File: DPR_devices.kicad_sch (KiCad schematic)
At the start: 0 parts

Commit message: Added all 3 ADC and routed them to RP2040 !
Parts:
- added C37, C40, C41, C42, C45, C46, C47, C50, C51: 1u, symbol Device:C
- added C38, C43, C48: 10u, symbol Device:C
- added C39, C44, C49: 4.7u, symbol Device:C
- added U7, U8, U9: ADS8681IPW, symbol DPR_devices:ADS8681IPW_
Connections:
- new net: C47.1, C48.2, U9.6 (REFCAP)
- new net: C47.2, U9.5 (REFGND)
- new net: C37.1, C38.2, U7.6 (REFCAP)
- new net: C37.2, U7.5 (REFGND)
- new net: C42.2, U8.5 (REFGND)
- new net: C42.1, C43.2, U8.6 (REFCAP)
- new net +3V3: C41.2, C46.2, C51.2, U7.16 (DVDD), U8.16 (DVDD), U9.16 (DVDD)
- new net +5V: C40.1, C45.1, C50.1, U7.2 (AVDD), U8.2 (AVDD), U9.2 (AVDD)
- new net ADC_REF: C39.1, C44.1, C49.1, U7.4 (REFIO), U8.4 (REFIO), U9.4 (REFIO)
- new net ADC_RESET: U7.9 (RST), U8.9 (RST), U9.9 (RST)
- new net CS_ADC1: U7.11 (CONVST/CS)
- new net CS_ADC2: U8.11 (CONVST/CS)
- new net CS_ADC3: U9.11 (CONVST/CS)
- new net GND: C38.1, C39.2, C40.2, C41.1, C43.1, C44.2, C45.2, C46.1, C48.1, C49.2, C50.2, C51.1, U7.1 (DGND), U7.3 (AGND), U7.8 (AIN_GND), U8.1 (DGND), U8.3 (AGND), U8.8 (AIN_GND), U9.1 (DGND), U9.3 (AGND), U9.8 (AIN_GND)
- new net MISO: U7.13 (SDO-0), U8.13 (SDO-0), U9.13 (SDO-0)
- new net MOSI: U7.10 (SDI), U8.10 (SDI), U9.10 (SDI)
- new net PD_OUT: U7.7 (AIN_P), U8.7 (AIN_P), U9.7 (AIN_P)
- new net SCLK: U7.12 (SCLK), U8.12 (SCLK), U9.12 (SCLK)
- no-connect marks 0 -> 6

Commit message: Last CPR_devices changes
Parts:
- added C52, C53, C54: 4.7n, symbol Device:C
- added J10: M12_P2, symbol Connector:Conn_01x04_Socket
- added J11: SMA_P3, symbol Connector:Conn_Coaxial
- added J6: M12_P1, symbol Connector:Conn_01x04_Socket
- added J7: M12_P3, symbol Connector:Conn_01x04_Socket
- added J8: SMA_P1, symbol Connector:Conn_Coaxial
- added J9: SMA_P2, symbol Connector:Conn_Coaxial
- added R10, R11, R12: 100R, symbol DPR_devices:R
- added U10: PCA9548APW, Package_SO:TSSOP-24_4.4x7.8mm_P0.65mm, symbol Interface_Expansion:PCA9548APW
- C37, C40, C41, C42, C45, C46, C47, C50, C51: value 1u -> C; footprint (none) -> Capacitor_SMD:C_0402_1005Metric; symbol Device:C -> DPR_devices:C
- C38, C43, C48: value 10u -> C; footprint (none) -> Capacitor_SMD:C_0603_1608Metric; symbol Device:C -> DPR_devices:C
- C39, C44, C49: value 4.7u -> C; footprint (none) -> Capacitor_SMD:C_0603_1608Metric; symbol Device:C -> DPR_devices:C
- U7, U8, U9: footprint (none) -> Package_SO:TSSOP-16_4.4x5mm_P0.65mm
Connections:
- removed net PD_OUT: U7.7 (AIN_P), U8.7 (AIN_P), U9.7 (AIN_P)
- new net +24V: J10.1 (Pin_1), J6.1 (Pin_1), J7.1 (Pin_1)
- new net AGND: C52.1, C53.1, C54.1, J10.3 (Pin_3), J11.2 (Ext), J6.3 (Pin_3), J7.3 (Pin_3), J8.2 (Ext), J9.2 (Ext)
- new net AIN1_P: C52.2, J8.1 (In), R10.2, U7.7 (AIN_P)
- new net AIN2_P: C53.2, J9.1 (In), R11.2, U8.7 (AIN_P)
- new net AIN3_P: C54.2, J11.1 (In), R12.2, U9.7 (AIN_P)
- new net P1_OUT: J6.4 (Pin_4), R10.1
- new net P2_OUT: J10.4 (Pin_4), R11.1
- new net P3_OUT: J7.4 (Pin_4), R12.1
- no-connect marks 6 -> 9

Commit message: Schematic ok (je crois)
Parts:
- added C55: 100n, symbol Device:C
- added J12: Sens. PTE1, symbol Connector:Conn_01x04_Socket
- added J13: Sens. PTE2, symbol Connector:Conn_01x04_Socket
- added J14: Sens. PTE3, symbol Connector:Conn_01x04_Socket
- added R13, R14: 4.7k, symbol DPR_devices:R
- added R22: 10k, symbol DPR_devices:R
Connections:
- net +3V3: now also U10.24 (VCC), C55.2, J12.1 (Pin_1), J13.1 (Pin_1), J14.1 (Pin_1), R13.1, R14.1, R22.1
- net AGND: no longer J10.3 (Pin_3), J6.3 (Pin_3), J7.3 (Pin_3)
- net GND: now also U10.1 (A0), U10.12 (GND), U10.2 (A1), U10.21 (A2), C55.1, J12.2 (Pin_2), J13.2 (Pin_2), J14.2 (Pin_2)
- net I2C_SCL: now reaches U10.22 (SCL)
- net I2C_SCL: now also R13.2
- net I2C_SDA: now reaches U10.23 (SDA)
- net I2C_SDA: now also R14.2
- net at U10.3 (~{RESET}): now also R22.2
- net PTE1_SDA: now reaches U10.4 (SD0)
- net PTE1_SDA: now also J12.4 (Pin_4)
- net PTE1_SCL: now reaches U10.5 (SC0)
- net PTE1_SCL: now also J12.3 (Pin_3)
- net PTE2_SDA: now reaches U10.6 (SD1)
- net PTE2_SDA: now also J13.4 (Pin_4)
- net PTE2_SCL: now reaches U10.7 (SC1)
- net PTE2_SCL: now also J13.3 (Pin_3)
- net PTE3_SDA: now reaches U10.8 (SD2)
- net PTE3_SDA: now also J14.4 (Pin_4)
- net PTE3_SCL: now reaches U10.9 (SC2)
- net PTE3_SCL: now also J14.3 (Pin_3)
- new net GNDD: J10.3 (Pin_3), J6.3 (Pin_3), J7.3 (Pin_3)
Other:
- note added: "ADC x3"
- note added: "Conn. M12 pour Kistler analogique"
- note added: "Multiplexer + Conn. Sensata en I2C"
- note added: "SMA pour oscillo. p.ex"
- moved on the sheet: C37, C38, C39, C40, C41, C42, C43, C44, C45, C46, C47, C48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

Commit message: Last Push pour que tu check, après je commence le Layout
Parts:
- removed J10: M12_P2, symbol Connector:Conn_01x04_Socket
- removed J12: Sens. PTE1, symbol Connector:Conn_01x04_Socket
- removed J13: Sens. PTE2, symbol Connector:Conn_01x04_Socket
- removed J14: Sens. PTE3, symbol Connector:Conn_01x04_Socket
- removed J6: M12_P1, symbol Connector:Conn_01x04_Socket
- removed J7: M12_P3, symbol Connector:Conn_01x04_Socket
- added J12: Sens. P2, KiNic_footprints:M12B05PFFREE0001, symbol KiNic_symbols:M12B-05PFFR-EE0001
- added J13: Sens. P3, KiNic_footprints:M12B05PFFREE0001, symbol KiNic_symbols:M12B-05PFFR-EE0001
- added J17: Sens. P1, KiNic_footprints:M12B05PFFREE0001, symbol KiNic_symbols:M12B-05PFFR-EE0001
- added J6: M12_P1, DPR_devices:M12_NorComp_4Pin_RA, symbol Connector:Conn_01x05_Socket
- added J7: M12_P2, DPR_devices:M12_NorComp_4Pin_RA, symbol Connector:Conn_01x05_Socket
- added J8: M12_P3, DPR_devices:M12_NorComp_4Pin_RA, symbol Connector:Conn_01x05_Socket
- C37, C40, C41, C42, C45, C46, C47, C50, C51: value C -> 1u
- C38, C43, C48: value C -> 10u
- C39, C44, C49: value C -> 4.7u
- C52, C53, C54, C55: footprint (none) -> Capacitor_SMD:C_0402_1005Metric
- J10: renamed from J9; footprint (none) -> Connector_Coaxial:SMA_Amphenol_901-144_Vertical
- J11: footprint (none) -> Connector_Coaxial:SMA_Amphenol_901-144_Vertical
- J9: renamed from J8; footprint (none) -> Connector_Coaxial:SMA_Amphenol_901-144_Vertical
- R10, R11, R12, R13, R14, R22: footprint (none) -> Resistor_SMD:R_0603_1608Metric
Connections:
- net +24V: now also J6.1 (Pin_1), J7.1 (Pin_1), J8.1 (Pin_1)
- net +5V: now also J12.4, J13.4, J17.4
- net GNDD: now also J12.3, J12.5, J13.3, J13.5, J17.3, J17.5, J6.3 (Pin_3), J6.5 (Pin_5), J7.3 (Pin_3), J7.5 (Pin_5), J8.3 (Pin_3), J8.5 (Pin_5)
- net P1_OUT: now also J6.4 (Pin_4)
- net P2_OUT: now also J7.4 (Pin_4)
- net P3_OUT: now also J8.4 (Pin_4)
- net PTE1_SCL: now also J17.1
- net PTE1_SDA: now also J17.2
- net PTE2_SCL: now also J12.1
- net PTE2_SDA: now also J12.2
- net PTE3_SCL: now also J13.1
- net PTE3_SDA: now also J13.2
- no-connect marks 9 -> 19
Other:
- note added: "SMA (?)"
- note removed: "SMA pour oscillo. p.ex"
- moved on the sheet: C52, C53, C54, J10, J11, J9, R10, R11, R12

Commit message: Finito je te laisse check
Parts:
- removed J6: M12_P1, DPR_devices:M12_NorComp_4Pin_RA, symbol Connector:Conn_01x05_Socket
- removed J7: M12_P2, DPR_devices:M12_NorComp_4Pin_RA, symbol Connector:Conn_01x05_Socket
- removed J8: M12_P3, DPR_devices:M12_NorComp_4Pin_RA, symbol Connector:Conn_01x05_Socket
- added H2, H3, H4: MountingHole, MountingHole:MountingHole_3.2mm_M3, symbol Mechanical:MountingHole
- added J14: Servo1, Connector_PinHeader_2.54mm:PinHeader_1x03_P2.54mm_Vertical, symbol Connector:Conn_01x03_Pin
- added J16: Servo2, Connector_PinHeader_2.54mm:PinHeader_1x03_P2.54mm_Vertical, symbol Connector:Conn_01x03_Pin
- added J20: M12_P2, KiNic_footprints:M12B05PFFREE0001, symbol KiNic_symbols:M12B-05PFFR-EE0001
- added J6: M12_P3, KiNic_footprints:M12B05PFFREE0001, symbol KiNic_symbols:M12B-05PFFR-EE0001
- added J7: M12_P1, KiNic_footprints:M12B05PFFREE0001, symbol KiNic_symbols:M12B-05PFFR-EE0001
- added R23, R24, R25, R26, R27, R28: 4.7k, Resistor_SMD:R_0603_1608Metric, symbol DPR_devices:R
- added R30, R31: 47R, Resistor_SMD:R_0603_1608Metric, symbol DPR_devices:R
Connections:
- net +24V: now also J20.4, J6.4, J7.4
- net +3V3: now also J12.1, J12.2, J13.1, J13.2, J17.1, J17.2, R23.2, R24.2, R25.2, R26.2, R27.2, R28.2
- net GNDD: now also J20.3, J20.5, J6.3, J6.5, J7.3, J7.5
- net P1_OUT: now also J7.1
- net P2_OUT: now also J20.1
- net P3_OUT: now also J6.1
- net PTE1_SCL: now also R27.1; no longer J17.1
- net PTE1_SDA: now also R28.1; no longer J17.2
- net PTE2_SCL: now also R23.1; no longer J12.1
- net PTE2_SDA: now also R24.1; no longer J12.2
- net PTE3_SCL: now also R25.1; no longer J13.1
- net PTE3_SDA: now also R26.1; no longer J13.2
- net RESET: now reaches R22.2, U10.3 (~{RESET})
- new net: J14.3 (Pin_3), R30.1
- new net: J16.3 (Pin_3), R31.1
- new net +8V4_SERVO: J14.2 (Pin_2), J16.2 (Pin_2)
- new net GND_SERVO: J14.1 (Pin_1), J16.1 (Pin_1)
- new net PWM_SERVO1: R30.2
- new net PWM_SERVO2: R31.2
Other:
- note added: "M3"
- note added: "SMA"
- note removed: "SMA (?)"
- moved on the sheet: C55, J12, J13, J17, R13, R14, R22, U10

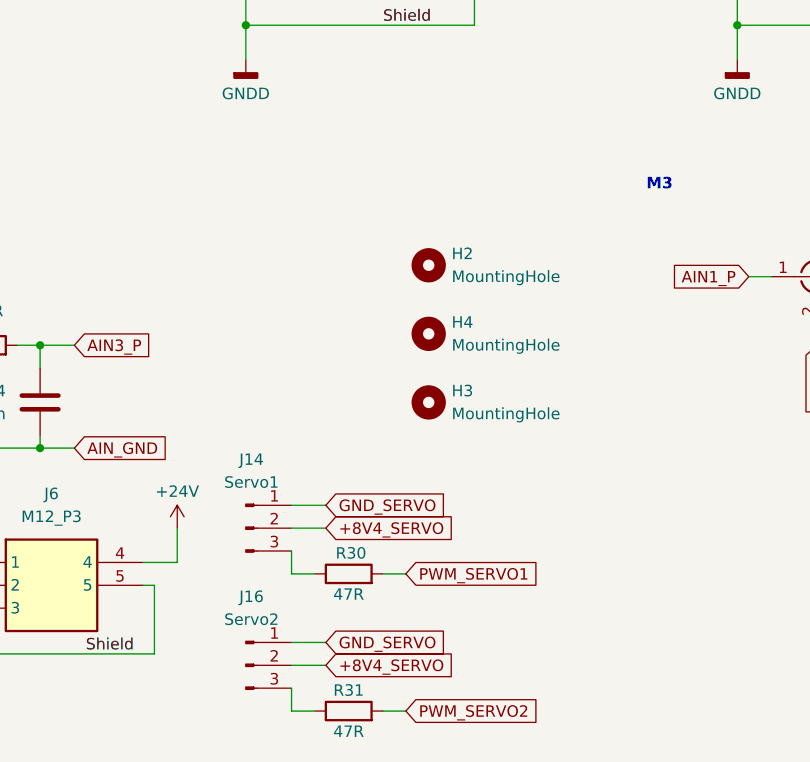
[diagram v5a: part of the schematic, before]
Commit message: added reset and bootsel buttons
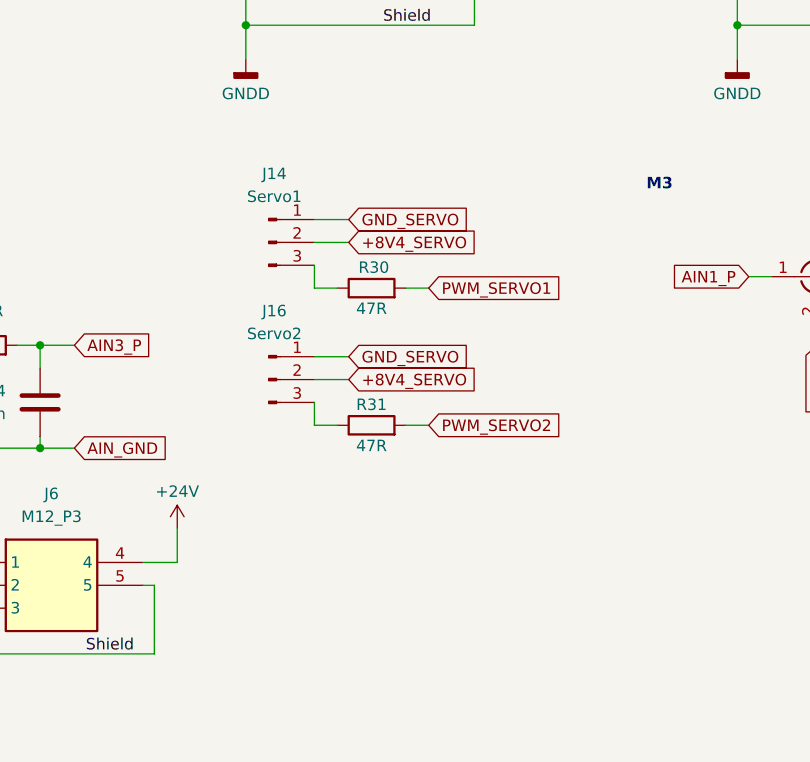
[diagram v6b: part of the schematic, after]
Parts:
- removed H2, H3, H4: MountingHole, MountingHole:MountingHole_3.2mm_M3, symbol Mechanical:MountingHole
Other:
- moved on the sheet: J14, J16, R30, R31

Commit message: last modifications
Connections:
- net AGND is gone; now on net GND: C52.1, C53.1, C54.1, J10.2 (Ext), J11.2 (Ext), J9.2 (Ext)

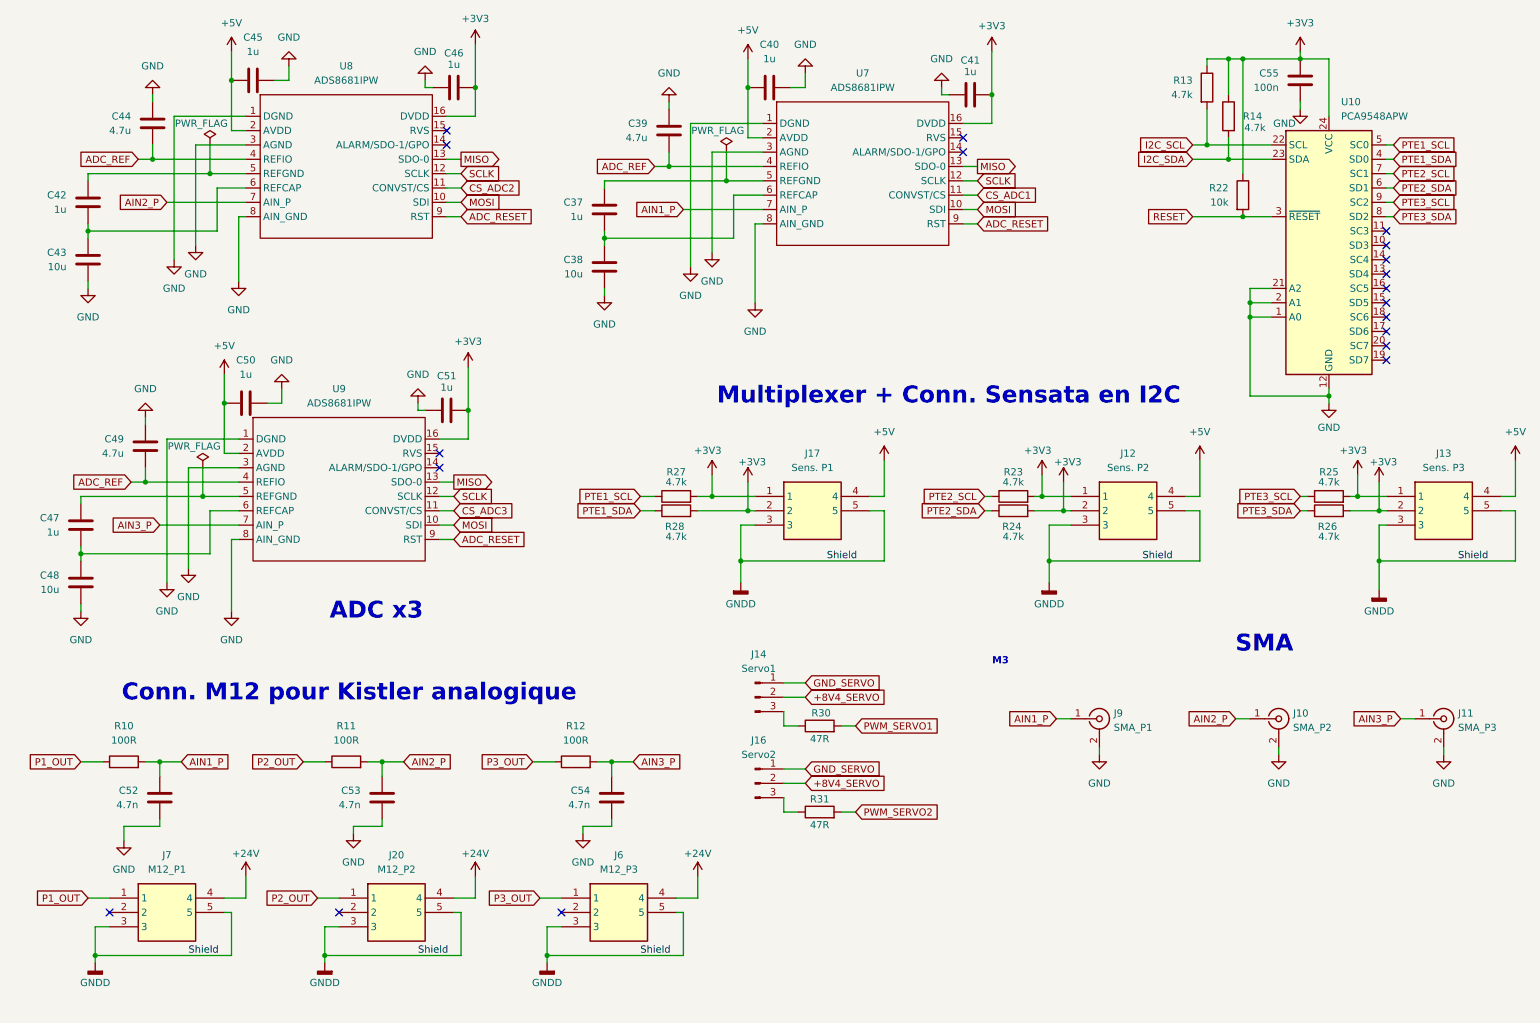
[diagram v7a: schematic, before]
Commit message: Changed M12 for SMA + 2 pins alim. --> we will have to split the cable from Kistlers
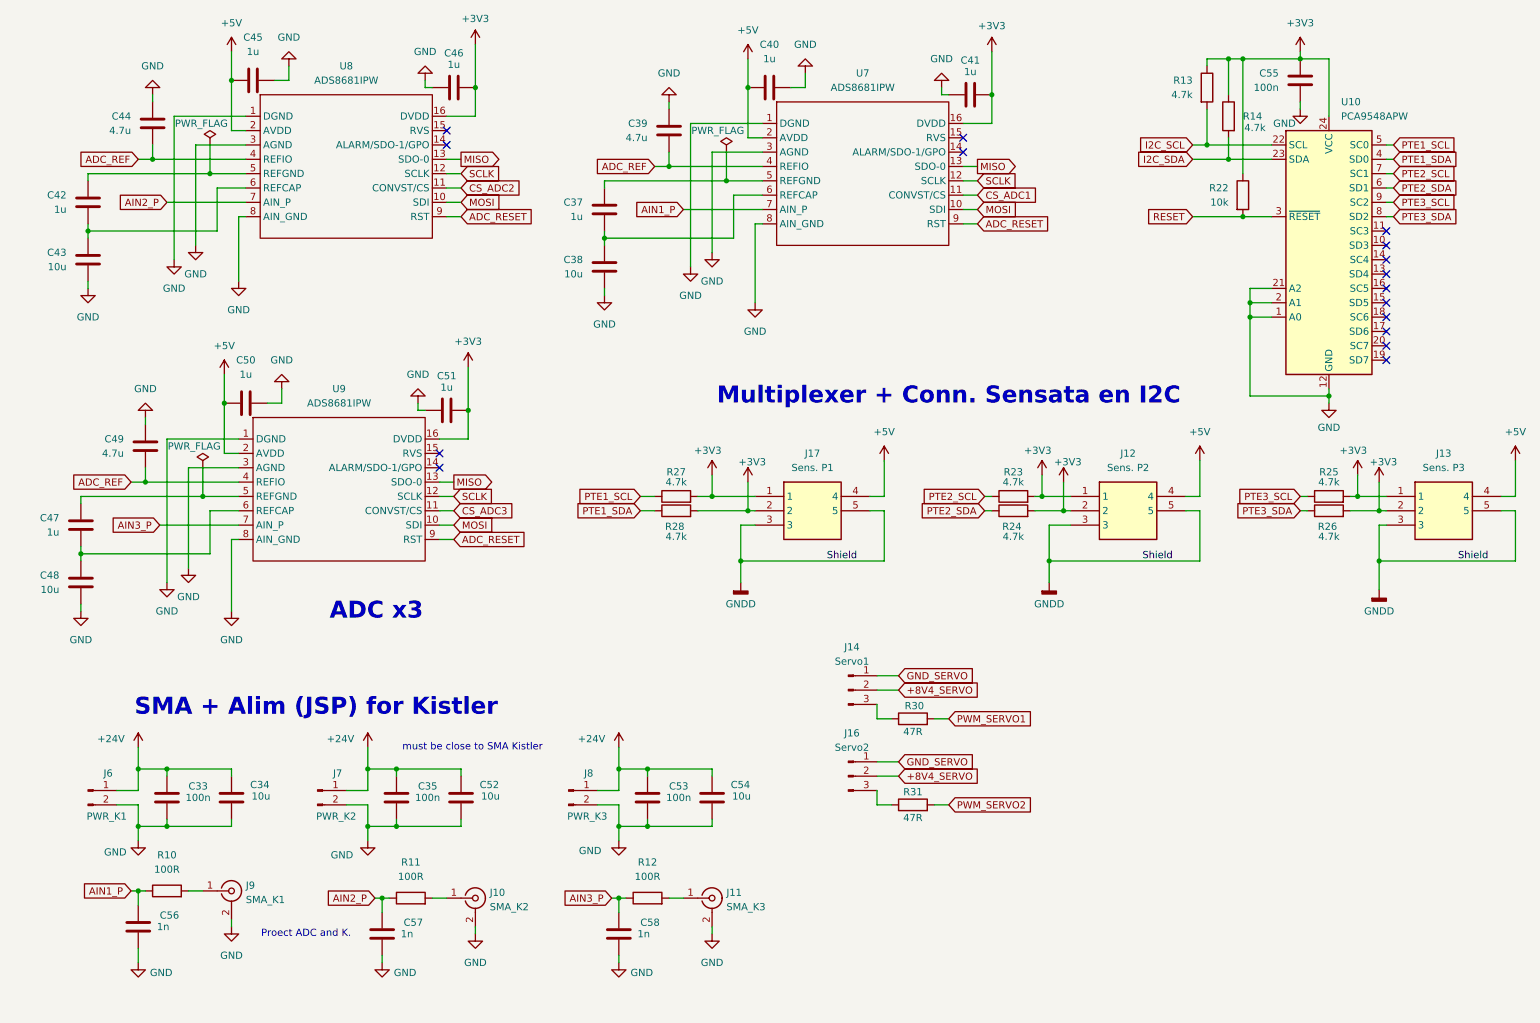
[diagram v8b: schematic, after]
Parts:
- removed J20: M12_P2, KiNic_footprints:M12B05PFFREE0001, symbol KiNic_symbols:M12B-05PFFR-EE0001
- removed J6: M12_P3, KiNic_footprints:M12B05PFFREE0001, symbol KiNic_symbols:M12B-05PFFR-EE0001
- removed J7: M12_P1, KiNic_footprints:M12B05PFFREE0001, symbol KiNic_symbols:M12B-05PFFR-EE0001
- removed R10, R11, R12: 100R, Resistor_SMD:R_0603_1608Metric, symbol DPR_devices:R
- added C33, C35: 100n, Capacitor_SMD:C_0402_1005Metric, symbol Device:C
- added C34: 10u, Capacitor_SMD:C_0805_2012Metric, symbol Device:C
- added C56, C57, C58: 1n, Capacitor_SMD:C_0603_1608Metric, symbol Device:C
- added J6: PWR_K1, Connector_JST:JST_GH_BM02B-GHS-TBT_1x02-1MP_P1.25mm_Vertical, symbol Connector:Conn_01x02_Pin
- added J7: PWR_K2, Connector_JST:JST_GH_BM02B-GHS-TBT_1x02-1MP_P1.25mm_Vertical, symbol Connector:Conn_01x02_Pin
- added J8: PWR_K3, Connector_JST:JST_GH_BM02B-GHS-TBT_1x02-1MP_P1.25mm_Vertical, symbol Connector:Conn_01x02_Pin
- added R10, R11, R12: 100R, Resistor_SMD:R_0603_1608Metric, symbol Device:R
- C52, C54: value 4.7n -> 10u; footprint Capacitor_SMD:C_0402_1005Metric -> Capacitor_SMD:C_0805_2012Metric
- C53: value 4.7n -> 100n
- J10: value SMA_P2 -> SMA_K2
- J11: value SMA_P3 -> SMA_K3
- J9: value SMA_P1 -> SMA_K1
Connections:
- net +24V: now also C52.1, C53.1, C54.1, C33.1, C34.1, C35.1, J6.1 (Pin_1), J7.1 (Pin_1), J8.1 (Pin_1)
- net AIN1_P: now also C56.1, R10.1; no longer C52.2, J9.1 (In)
- net AIN2_P: now also C57.1, R11.1; no longer C53.2, J10.1 (In)
- net AIN3_P: now also C58.1, R12.1; no longer C54.2, J11.1 (In)
- net GND: now also C52.2, C53.2, C54.2, C33.2, C34.2, C35.2, C56.2, C57.2, C58.2, J6.2 (Pin_2), J7.2 (Pin_2), J8.2 (Pin_2); no longer C52.1, C53.1, C54.1
- new net: J10.1 (In), R11.2
- new net: J11.1 (In), R12.2
- new net: J9.1 (In), R10.2
- no-connect marks 19 -> 16
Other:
- note added: "Proect ADC and K."
- note added: "SMA + Alim (JSP) for Kistler"
- note added: "must be close to SMA Kistler"
- note removed: "Conn. M12 pour Kistler analogique"
- note removed: "M3"
- note removed: "SMA"
- moved on the sheet: J14, J16, J9, R30, R31
